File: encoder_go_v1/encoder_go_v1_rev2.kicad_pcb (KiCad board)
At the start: 2 copper layers, 25 x 25 mm, 7 parts, among them J1 BM05B-SRSS-TB_LF__SN_, J2 optional features, U1 MT6701-SOP8

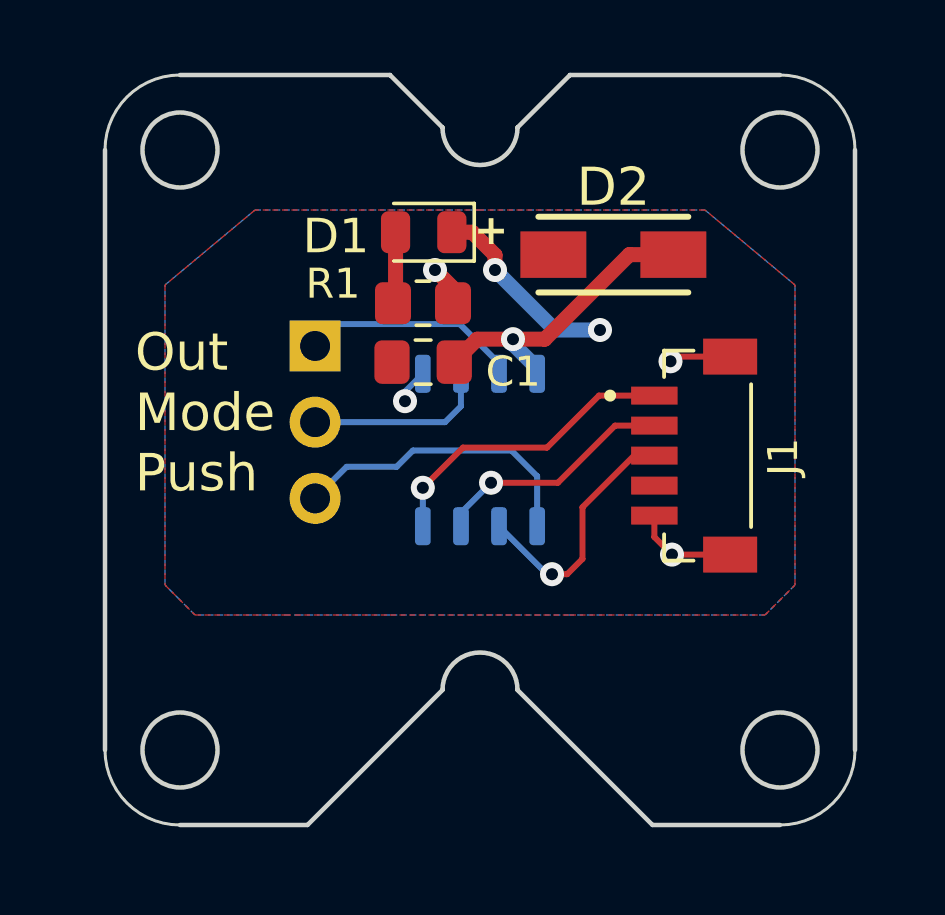
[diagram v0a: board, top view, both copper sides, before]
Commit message: remove unused files and edited pcb for cnc mill process
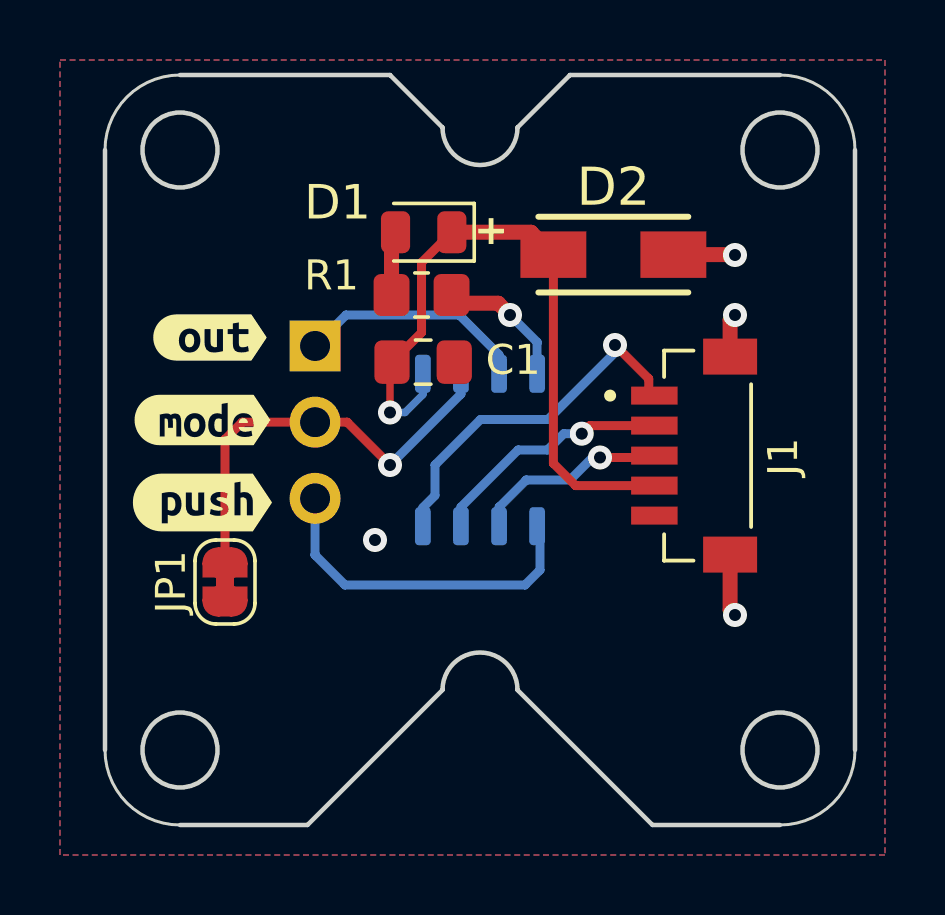
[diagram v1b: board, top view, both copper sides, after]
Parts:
- added JP1: SolderJumper_2_Bridged, Jumper:SolderJumper-2_P1.3mm_Bridged_RoundedPad1.0x1.5mm, F.Cu at (141.5, 104.4)
- added kibuzzard-6941C974: G***, kibuzzard-6941C974, B.Cu at (159.2, 99.0)
- added kibuzzard-69442F0D: G***, kibuzzard-69442F0D, F.Cu at (141.0, 96.2)
- added kibuzzard-69442F26: G***, kibuzzard-69442F26, F.Cu at (140.8, 99.0)
- added kibuzzard-69442F34: G***, kibuzzard-69442F34, F.Cu at (140.8, 101.8)
- R1: value 1k -> 2k
- moved R1 0.28 mm to (148.1, 94.8)
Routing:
- net +3.3V: track 7.74 -> 23.2 mm, vias 3 -> 1
- net Net-(J2-Pin_2): track 6.16 -> 14.5 mm, vias 0 -> 1
- net GND: track 17.2 -> 10.2 mm, vias 4 -> 5
- net CS: track 10.3 -> 12.2 mm
- net SDA: track 8.49 -> 6.52 mm
- net Net-(J2-Pin_3): track 10.1 -> 11.5 mm
- added copper zone on F.Cu, net GND
- removed copper zone on F.Cu, net +3.3V
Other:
- board text removed: "EncoderGo V1.R2 :)"
- board text removed: "Out Mode Push"

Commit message: adjust silkscreen
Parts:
- removed kibuzzard-6941C974: G***, kibuzzard-6941C974
- added kibuzzard-69640B5A: G***, kibuzzard-69640B5A, B.Cu at (159.2, 100.0)
